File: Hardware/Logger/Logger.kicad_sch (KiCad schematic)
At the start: 0 parts

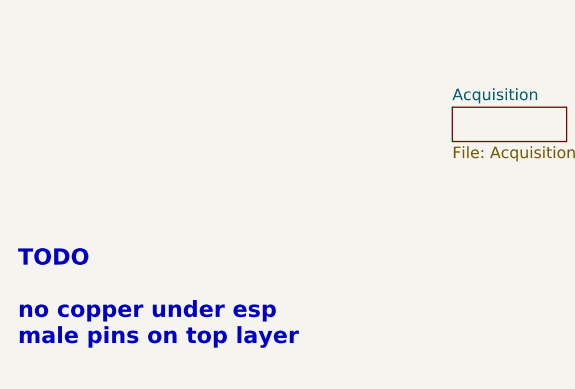
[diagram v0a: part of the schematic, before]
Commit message: add on silkscreen icons to describe purpouse of buttons
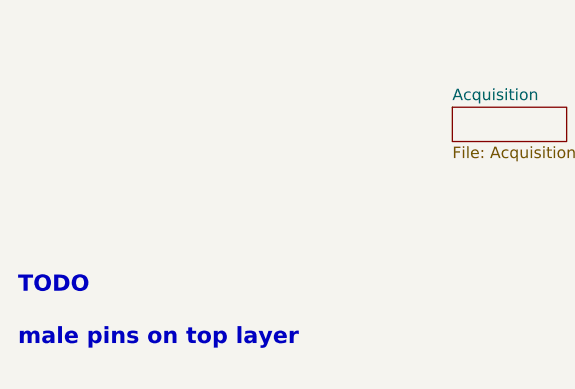
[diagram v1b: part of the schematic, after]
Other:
- note added: "TODO male pins on top layer"
- note removed: "TODO no copper under esp male pins on top layer"
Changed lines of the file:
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@@
 (kicad_sch (version 20210621) (generator eeschema)
   (paper "A4")
-  (text "TODO\n\nno copper under esp\nmale pins on top layer" (at 96.52 101.6 0)
+  (text "TODO\n\nmale pins on top layer" (at 96.52 101.6 0)
     (effects (font (size 1.8034 1.8034) (thickness 0.3607) bold) (justify left bottom))
   )
